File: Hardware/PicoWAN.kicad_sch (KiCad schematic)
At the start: 49 parts, among them J1 Battery, J2 SWD, J3 Conn_left, J4 Conn_right, P1 USB_C_Plug_USB2.0, Q1 DMG3415U-7, SW1 BOOT, SW2 RESET, U1 AP2112K-3.3, U2 RP2040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

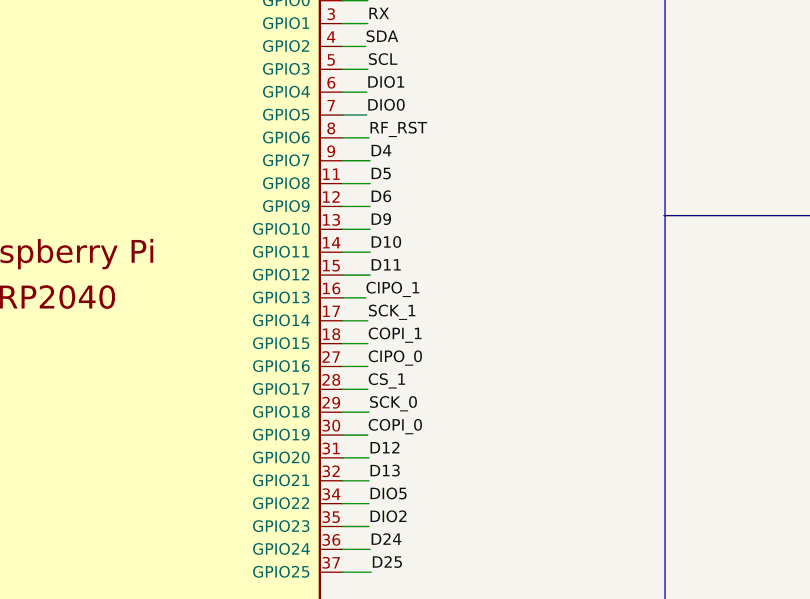
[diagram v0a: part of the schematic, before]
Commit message: change pins SPI ok
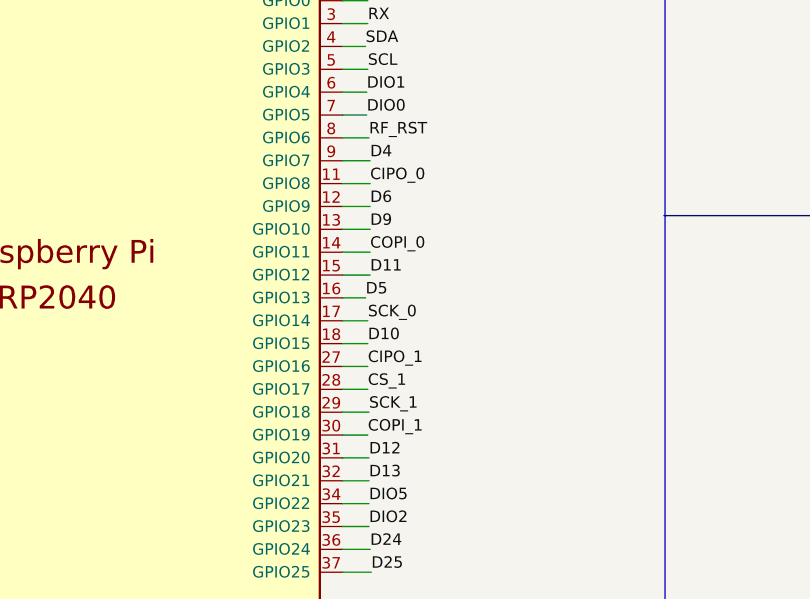
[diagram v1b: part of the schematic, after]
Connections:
- net CIPO_0: now also U2.11 (GPIO8); no longer U2.27 (GPIO16)
- net CIPO_1: now also U2.27 (GPIO16); no longer U2.16 (GPIO13)
- net COPI_0: now also U2.14 (GPIO11); no longer U2.30 (GPIO19)
- net COPI_1: now also U2.30 (GPIO19); no longer U2.18 (GPIO15)
- net D10: now also U2.18 (GPIO15); no longer U2.14 (GPIO11)
- net D5: now also U2.16 (GPIO13); no longer U2.11 (GPIO8)
- net SCK_0: now also U2.17 (GPIO14); no longer U2.29 (GPIO18)
- net SCK_1: now also U2.29 (GPIO18); no longer U2.17 (GPIO14)
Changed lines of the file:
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@@
   (title_block
     (title "PicoWAN")
-    (date "2021-01-30")
-    (rev "1.0")
+    (date "2022-07-15")
+    (rev "1.1")
     (company "ElectronicCats")
     (comment 4 "Andres Sabas")
@@
     (effects (font (size 1.27 1.27)) (justify left bottom))
   )
-  (label "CIPO_1" (at 118.11 88.773 0)
+  (label "CIPO_1" (at 118.364 96.393 0)
     (effects (font (size 1.27 1.27)) (justify left bottom))
   )
@@
     (effects (font (size 1.27 1.27)) (justify left bottom))
   )
-  (label "D5" (at 118.618 76.073 0)
+  (label "D5" (at 118.11 88.773 0)
     (effects (font (size 1.27 1.27)) (justify left bottom))
   )
@@
     (effects (font (size 1.27 1.27)) (justify right bottom))
   )
-  (label "SCK_0" (at 118.491 101.473 0)
+  (label "SCK_0" (at 118.364 91.313 0)
     (effects (font (size 1.27 1.27)) (justify left bottom))
   )
@@
     (effects (font (size 1.27 1.27)) (justify left bottom))
   )
-  (label "COPI_1" (at 118.364 93.853 0)
+  (label "COPI_1" (at 118.364 104.013 0)
     (effects (font (size 1.27 1.27)) (justify left bottom))
   )
@@
     (effects (font (size 1.27 1.27)) (justify left bottom))
   )
-  (label "COPI_0" (at 118.364 104.013 0)
+  (label "COPI_0" (at 118.618 83.693 0)
     (effects (font (size 1.27 1.27)) (justify left bottom))
   )
@@
     (effects (font (size 1.27 1.27)) (justify left bottom))
   )
-  (label "SCK_1" (at 118.364 91.313 0)
-    (effects (font (size 1.27 1.27)) (justify left bottom))
-  )
-  (label "D10" (at 118.618 83.693 0)
+  (label "SCK_1" (at 118.491 101.473 0)
+    (effects (font (size 1.27 1.27)) (justify left bottom))
+  )
+  (label "D10" (at 118.364 93.853 0)
     (effects (font (size 1.27 1.27)) (justify left bottom))
   )
@@
     (effects (font (size 1.27 1.27)) (justify left bottom))
   )
-  (label "CIPO_0" (at 118.364 96.393 0)
-    (effects (font (size 1.27 1.27)) (justify left bottom))
-  )
+  (label "CIPO_0" (at 118.618 76.073 0)
+    (effects (font (size 1.27 1.27)) (justify left bottom))
+  )
